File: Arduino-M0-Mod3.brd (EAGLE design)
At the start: 68.6 x 53.3 mm, 111 parts, among them CN2 PINHEAD-2x5-P1.27, IC1 74LVC1G125DCKR, IC2 SAMD21G18A-AUT, IC3 MPM3610, IC4 MPM3810GQB-33, IC5 RTC_PCF8523T, IC6 EM4095, Y1 32.768kHz, Y4 32,768Khz

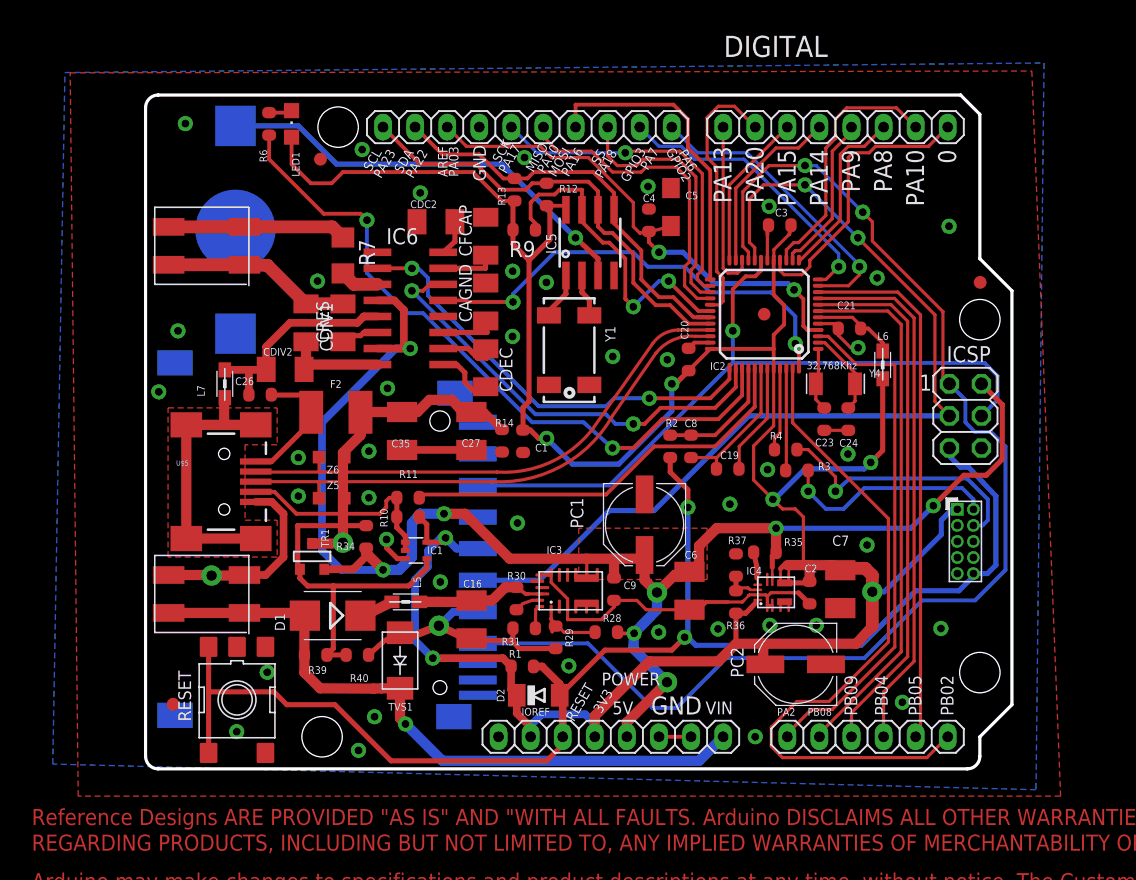
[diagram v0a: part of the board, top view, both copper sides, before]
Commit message: Mod3 traces complete
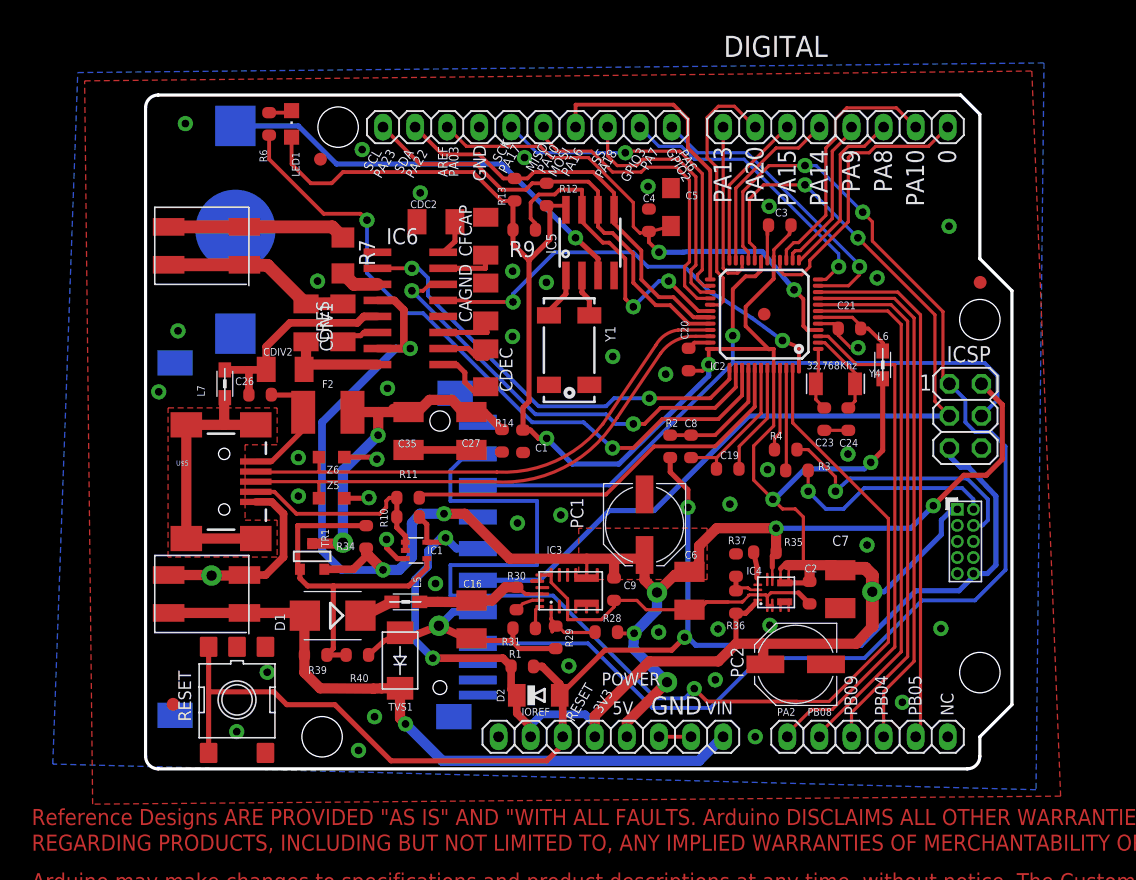
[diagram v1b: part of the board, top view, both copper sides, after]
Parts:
- removed TP_A5: TP_SP, SmartPrj:TP-SP
- moved F2 0.63 mm to (14.4, 28.2)
- moved C35 0.51 mm to (20.8, 26.7)
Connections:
- removed net PB02_AIN10: AD.6, IC2.47, TP_A5.X
- removed net SD_CS: U$4.1
- new net PB02_CS_SD: IC2.47, U$4.1
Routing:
- net PB02_CS_SD: track 0.00 -> 91.9 mm, vias 0 -> 1
- net PB02_AIN10: track 53.4 -> 0.00 mm
- net GND: track 118.4 -> 122.5 mm, vias 43 -> 44
- net +3V3: track 220.8 -> 224.0 mm
- net PB03_RFIDIN: track 36.3 -> 34.5 mm
- net USBVCC: track 26.7 -> 28.4 mm, vias 1 -> 2
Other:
- board text added: "NC"
- board text removed: "PB02"
